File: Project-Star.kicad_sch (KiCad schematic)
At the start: 8 parts, among them J1 Screw_Terminal_01x01, J2 Screw_Terminal_01x01, J3 Sense Terminals, J4 SMB, J5 Screw_Terminal_01x01, J6 Screw_Terminal_01x01, SW1 SW_DPST, SW2 SW_DPST

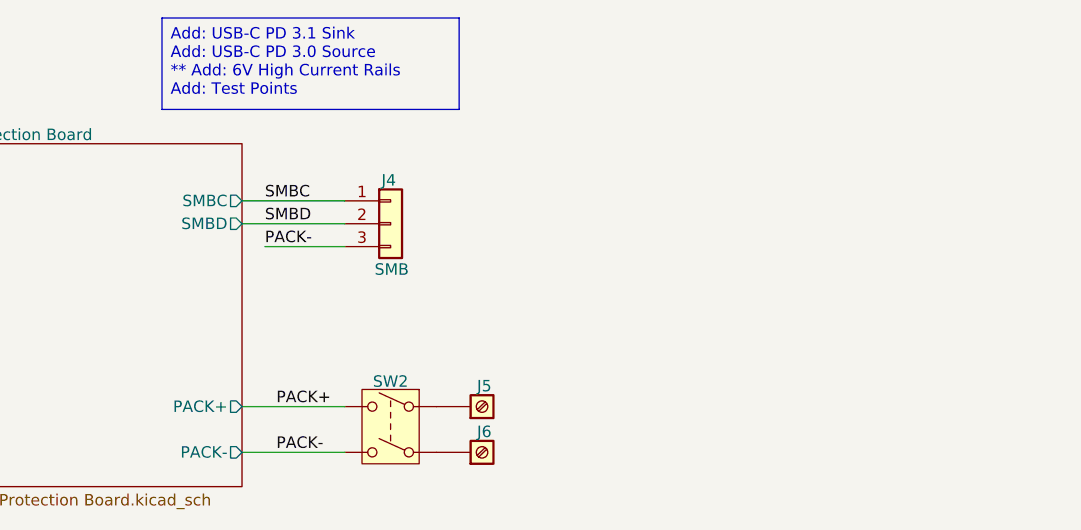
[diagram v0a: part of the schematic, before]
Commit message: I still need to add the 6V line and test points
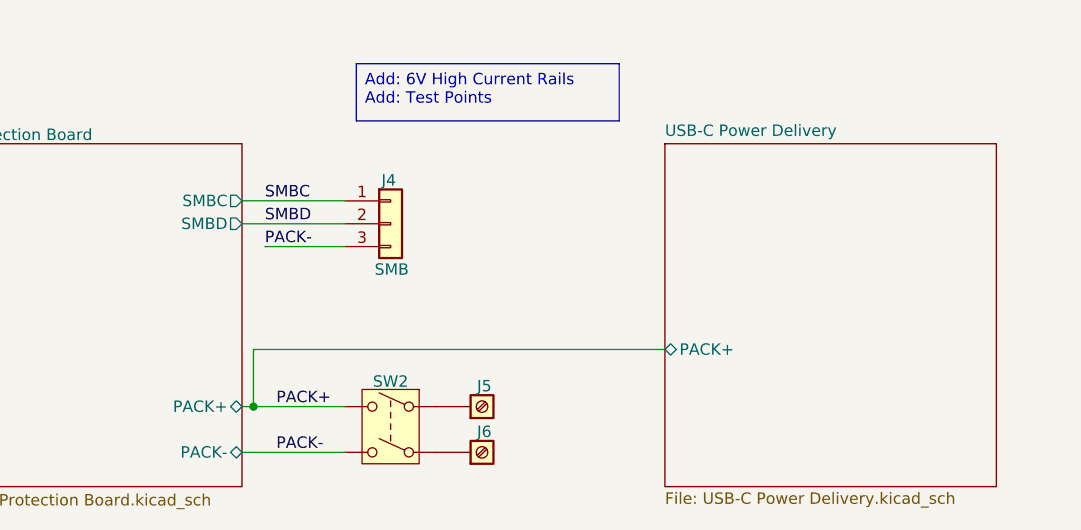
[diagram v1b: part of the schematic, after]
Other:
- added sheet USB-C Power Delivery (USB-C Power Delivery.kicad_sch)
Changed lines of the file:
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@@
 	(generator_version "9.0")
 	(paper "A4")
-	(text_box "   Add: USB-C PD 3.1 Sink\n   Add: USB-C PD 3.0 Source\n** Add: 6V High Current Rails\n   Add: Test Points"
+	(text_box "Add: 6V High Current Rails\nAdd: Test Points"
 		(exclude_from_sim no)
-		(at 81.28 63.5 0)
-		(size 33.02 10.16)
+		(at 102.87 68.58 0)
+		(size 29.21 6.35)
 		(margins 0.9525 0.9525 0.9525 0.9525)
 		(stroke
@@
 		)
 	)
-	(wire
-		(pts
-			(xy 90.17 106.68) (xy 101.6 106.68)
+	(junction
+		(at 91.44 106.68)
+		(diameter 0)
+		(color 0 0 0 0)
+	)
+	(wire
+		(pts
+			(xy 90.17 106.68) (xy 91.44 106.68)
 		)
 		(stroke
@@
 	(wire
 		(pts
+			(xy 91.44 100.33) (xy 137.16 100.33)
+		)
+		(stroke
+			(width 0)
+			(type default)
+		)
+	)
+	(wire
+		(pts
 			(xy 43.18 92.71) (xy 54.61 92.71)
 		)
@@
 	(wire
 		(pts
+			(xy 91.44 100.33) (xy 91.44 106.68)
+		)
+		(stroke
+			(width 0)
+			(type default)
+		)
+	)
+	(wire
+		(pts
 			(xy 43.18 97.79) (xy 54.61 97.79)
 		)
@@
 		(pts
 			(xy 43.18 82.55) (xy 54.61 82.55)
+		)
+		(stroke
+			(width 0)
+			(type default)
+		)
+	)
+	(wire
+		(pts
+			(xy 91.44 106.68) (xy 101.6 106.68)
 		)
 		(stroke
@@
 			)
 		)
-		(pin "PACK-" output
+		(pin "PACK-" bidirectional
 			(at 90.17 111.76 0)
 			(effects
@@
 			)
 		)
-		(pin "PACK+" output
+		(pin "PACK+" bidirectional
 			(at 90.17 106.68 0)
 			(effects
@@
 				)
 			)
+		)
+	)
+	(sheet
+		(at 137.16 77.47)
+		(size 36.83 38.1)
+		(exclude_from_sim no)
+		(in_bom yes)
+		(on_board yes)
+		(dnp no)
+		(fields_autoplaced yes)
+		(stroke
+			(width 0.1524)
+			(type solid)
+		)
+		(fill
+			(color 0 0 0 0.0000)
+		)
+		(property "Sheetname" "USB-C Power Delivery"
+			(at 137.16 76.7584 0)
+			(effects
+				(font
+					(size 1.27 1.27)
+				)
+				(justify left bottom)
+			)
+		)
+		(property "Sheetfile" "USB-C Power Delivery.kicad_sch"
+			(at 137.16 116.1546 0)
+			(effects
+				(font
+					(size 1.27 1.27)
+				)
+				(justify left top)
+			)
+		)
+		(pin "PACK+" bidirectional
+			(at 137.16 100.33 180)
+			(effects
+				(font
+					(size 1.27 1.27)
+				)
+				(justify left)
+			)
+		)
+		(instances
+			(project "Project-Star"
+				(path "/fc8533bc-25dd-4c20-9b4c-ffebebd6739b"
+					(page "12")
+				)
+			)

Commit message: in progress still
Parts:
- added J7: I2C, symbol Connector_Generic:Conn_01x03
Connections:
- new net LDO_3V3: J7.1 (Pin_1)
- new net SCL: J7.3 (Pin_3)
- new net SDA: J7.2 (Pin_2)
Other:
- added sheet 6V High Power Line (6V High Power Line.kicad_sch)
- sheet USB-C Power Delivery ports: added LDO_3V3, SCL, SDA; removed none
